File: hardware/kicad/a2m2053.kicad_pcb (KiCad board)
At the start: 2 copper layers, 100 x 110 mm, 46 parts, among them J1 DB-19 female R/A (daisy chain), J2 CN104 mechanism, J3 CN102 host (FROM HOST), J4 Eject button, J5 In-use LED, U1 SN74LVC8T245DWR, U2 SN74LVC8T245DWR, U3 SN74LVC8T245DWR, U4 SN74LVC8T245DWR, U5 SN74LVC8T245DWR

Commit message: fix(pcb): remove two dangling vias left from hand edits
Co-Authored-By: Claude Fable 5.1 <noreply@anthropic.com>
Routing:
- net +12V: track 99.3 -> 102.9 mm
- net /PH0_A: vias 1 -> 0
- net /LED_B: vias 1 -> 0
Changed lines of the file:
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@@
 	)
 	(via
-		(at 139.825 77.6609)
+		(at 139.8 74.2)
 		(size 1)
 		(drill 0.5)
@@
 	)
 	(segment
-		(start 139.825 77.6609)
-		(end 141.2 77.6609)
+		(start 141.2 77.6609)
+		(end 141.2 76.22)
 		(width 1)
 		(layer "B.Cu")
@@
 	)
 	(segment
-		(start 141.2 77.6609)
-		(end 170.5259 77.6609)
+		(start 128.92 74.22)
+		(end 126.38 74.22)
 		(width 1)
 		(layer "B.Cu")
@@
 	)
 	(segment
-		(start 128.92 74.22)
-		(end 126.38 74.22)
+		(start 141.2 76.22)
+		(end 139.2 74.22)
 		(width 1)
 		(layer "B.Cu")
@@
 	(segment
 		(start 131.46 74.22)
-		(end 134.9009 77.6609)
+		(end 139.2 74.22)
 		(width 1)
 		(layer "B.Cu")
@@
 	)
 	(segment
-		(start 180.5766 77.5855)
-		(end 170.6013 77.5855)
+		(start 171.459033 77.5855)
+		(end 169.825 75.951467)
 		(width 1)
 		(layer "B.Cu")
@@
 	)
 	(segment
-		(start 185.9106 72.2515)
-		(end 180.5766 77.5855)
+		(start 139.2 74.22)
+		(end 169.825 74.22)
+		(width 1)
+		(layer "B.Cu")
+		(net "+12V")
+	)
+	(segment
+		(start 169.825 75.951467)
+		(end 169.825 74.22)
 		(width 1)
 		(layer "B.Cu")
@@
 	)
 	(segment
-		(start 170.6013 77.5855)
-		(end 170.6013 75.8387)
+		(start 180.5766 77.5855)
+		(end 171.459033 77.5855)
+		(width 1)
+		(layer "B.Cu")
+		(net "+12V")
+	)
+	(segment
+		(start 185.9106 72.2515)
+		(end 180.5766 77.5855)
 		(width 1)
 		(layer "B.Cu")
@@
 	)
 	(segment
-		(start 170.6013 75.8387)
+		(start 172.22 74.22)
 		(end 175.39 71.05)
 		(width 1)
@@
 	)
 	(segment
-		(start 134.9009 77.6609)
-		(end 139.825 77.6609)
+		(start 169.825 74.22)
+		(end 172.22 74.22)
 		(width 1)
 		(layer "B.Cu")
@@
 	)
 	(segment
-		(start 170.5259 77.6609)
-		(end 170.6013 77.5855)
-		(width 1)
-		(layer "B.Cu")
-		(net "+12V")
-	)
-	(segment
 		(start 129.325 90.35)
 		(end 129.325 75.8598)
@@
 		(net "/PH0_A")
 	)
-	(via
-		(at 131.2678 144.9024)
-		(size 0.6)
-		(drill 0.3)
-		(layers "F.Cu" "B.Cu")
-		(net "/PH0_A")
-	)
 	(segment
 		(start 130.4121 143.47)
@@
 		(net "/LED_B")
 	)
-	(via
-		(at 137.4625 64.7169)
-		(size 0.6)
-		(drill 0.3)
-		(layers "F.Cu" "B.Cu")
-		(net "/LED_B")
-	)

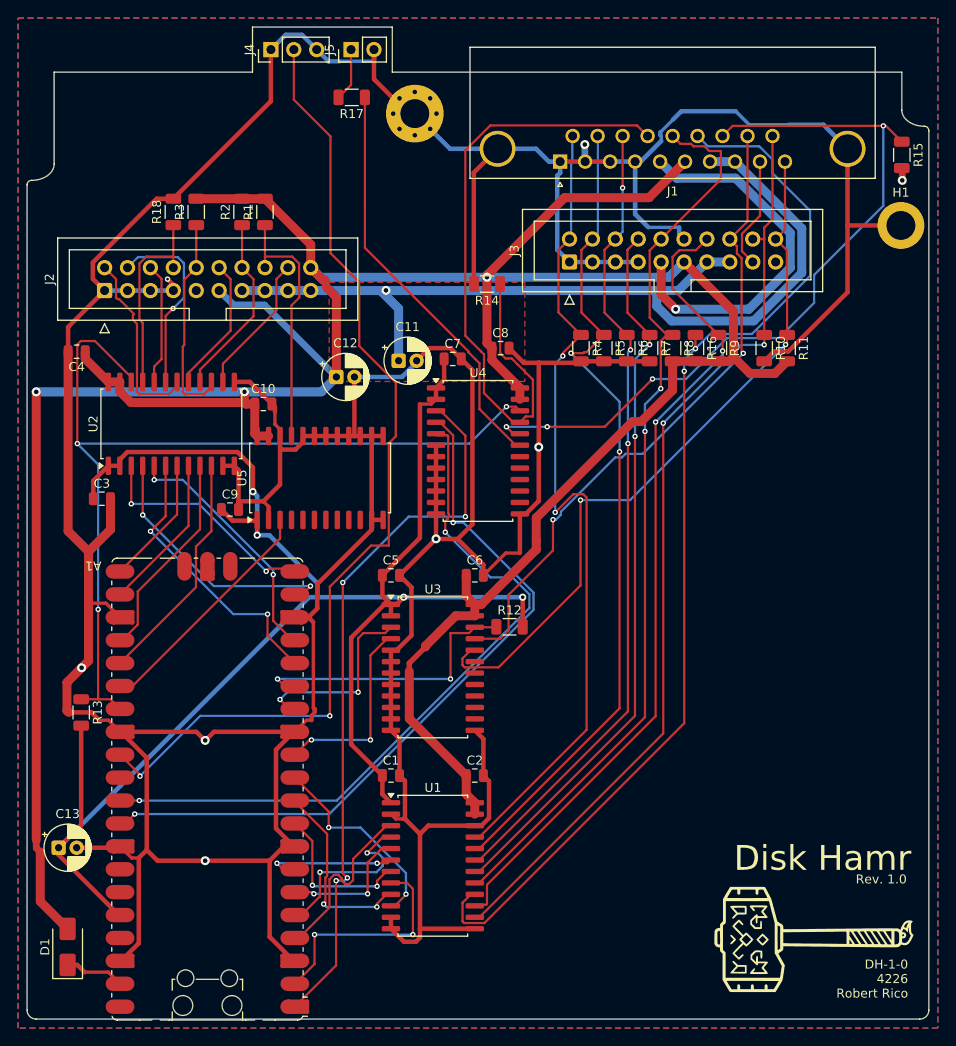
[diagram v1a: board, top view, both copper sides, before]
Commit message: feat(pcb): second layout of Disk Hamr rev 1.0, hand placed, +5V as traces
The 3D print put the mechanism header (J2) 11 mm too far from the
board edge, so the board was placed again by hand and re-routed with
Freerouting, then fixed up by hand.

- Shifters next to the connectors they serve: U2/U5 by J2, U1/U3/U4
  under J1/J3, Pico along the left edge.
- +5V pour on F.Cu removed. +5V is a Power net class now (1 mm
  track, 1 mm via) and is routed as traces; the pour had split into
  eleven islands under the signal traces and Freerouting treats a
  plane as already connected.
- +12V zone moved to B.Cu. GND stays a B.Cu plane; a fenced GND pocket
  under J1 is bridged with a top-side jumper.
- J4 (eject, 3-pin) and J5 (LED, 2-pin) swapped to the IF-83's order,
  shroud open toward the board edge. New TE AMP CT 2.00 mm footprints
  with the vendor STEP models (models are local, see docs/SOURCES.md).
- Logo footprint G1 re-placed from the library with the board-only
  attribute so Update PCB from Schematic leaves it alone.
- DRC with zone refill: 0 errors, 0 unconnected. 768 segments,
  123 vias.
- Top and bottom renders in hardware/kicad/render/.
- .gitignore: vendor 3D models and Freerouting .rules files.

Co-Authored-By: Claude Fable 5.1 <noreply@anthropic.com>
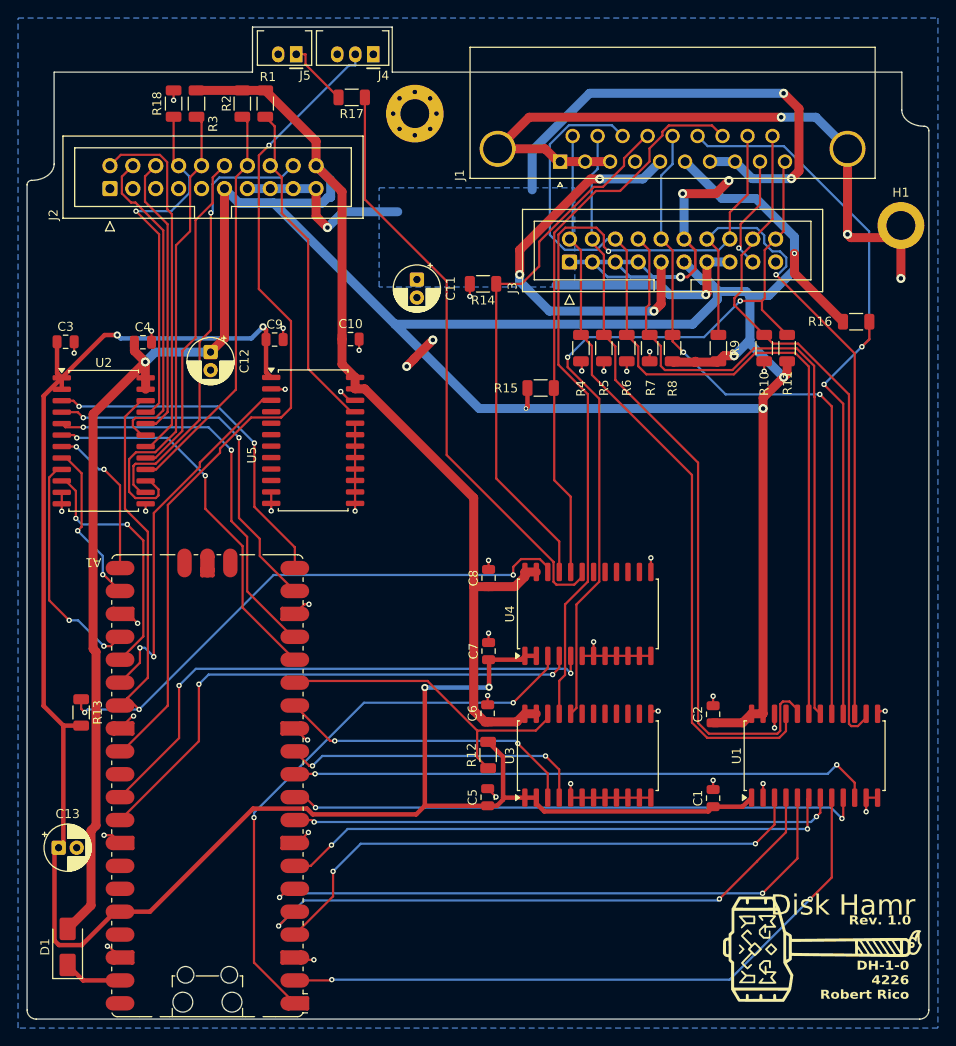
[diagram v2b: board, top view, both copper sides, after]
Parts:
- removed G1: logo_sm, a2m2053:logo_sm
- added G***: LOGO, a2m2053:logo_sm, F.Cu at (188.2, 147.2)
- J4: footprint Connector_PinHeader_2.54mm:PinHeader_1x03_P2.54mm_Vertical -> a2m2053:TE_AMP_CT_1x03_P2.00mm_Vertical
- J5: footprint Connector_PinHeader_2.54mm:PinHeader_1x02_P2.54mm_Vertical -> a2m2053:TE_AMP_CT_1x02_P2.00mm_Vertical
- moved R15 47.7 mm to (156.9, 85.0), turned to 180 degrees
- moved U1 44.1 mm to (187.3, 125.8), turned to 90 degrees
- moved C1 35.8 mm to (176.1, 130.5), turned to 90 degrees
- moved C7 32.6 mm to (151.2, 114.2), turned to 90 degrees
- moved C2 27.3 mm to (176.1, 121.2), turned to 90 degrees
- moved C5 26.8 mm to (151.1, 130.4), turned to 90 degrees
- moved C8 25.5 mm to (151.2, 106.1), turned to 90 degrees
- moved U4 21.8 mm to (162.2, 110.1), turned to 90 degrees
- moved U3 19.8 mm to (162.2, 125.8), turned to 90 degrees
- moved C9 19.5 mm to (127.5, 79.7)
- moved R16 18.1 mm to (191.9, 77.7), turned to 180 degrees
- moved C3 17.9 mm to (104.3, 79.9)
- moved C6 15.4 mm to (151.1, 121.1), turned to 90 degrees
- moved R12 14.4 mm to (151.1, 125.7), turned to 90 degrees
- moved C12 14.2 mm to (120.3, 81.0), turned to -90 degrees
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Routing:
- net GND: track 653.2 -> 212.4 mm, vias 7 -> 47
- net +5V: track 355.7 -> 436.2 mm, vias 4 -> 6
- net /PH2_A: track 14.8 -> 68.0 mm
- net /LASTONE_A: track 25.1 -> 73.1 mm
- net /PH1_A: track 19.8 -> 66.9 mm
- net /PH3_A: track 15.0 -> 62.1 mm
- net /WRREQ_A: track 17.5 -> 60.5 mm
- net /PH0_A: track 20.0 -> 62.9 mm, vias 0 -> 2
- net /WR_A: track 22.3 -> 65.0 mm
- net /HSTEN_A: track 21.5 -> 64.0 mm
- net /LASTONE: track 121.3 -> 83.0 mm
- net /MECH_WRTDATA: track 15.7 -> 49.7 mm, vias 0 -> 1
- net /MECH_WRTGATE: track 23.2 -> 52.5 mm
- net +3V3: track 197.7 -> 225.2 mm
- net /HOST_WR: track 103.3 -> 76.7 mm, vias 2 -> 0
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- added copper zone on B.Cu, net +12V
- removed copper zone on F.Cu, net +12V
- removed copper zone on F.Cu, net +5V

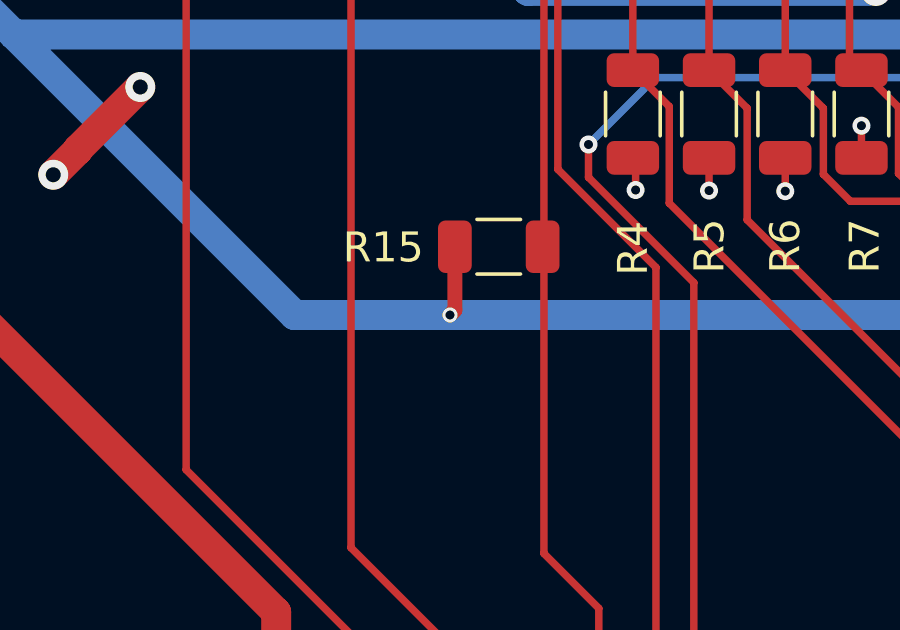
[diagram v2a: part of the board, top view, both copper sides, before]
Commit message: fix(pcb): R17 is 180 ohm, the IF-83's LED anode pull-up
Measured the LED pull-up on the IF-83: 180 ohm to +5V. Our board drives
the LED the same way (U4 output through R17, cathode to GND), so R17
takes the same value for the same brightness. About 17 mA from 5 V,
inside the 8T245's 32 mA output rating.

- Schematic and board: R17 value 330 -> 180. Footprint unchanged, so
  the fabrication outputs are unaffected.
- bom.csv / bom.md: R17 = 180 (Yageo RC1206FR-07180RL, DigiKey
  311-180FRCT-ND); the "keep 220 and 470 on hand" note is gone and the
  open item on the R17 value is closed.
- FABRICATION.md and research_notes.md record the measurement,
  2026-10-25.

Co-Authored-By: Claude Fable 5.1 <noreply@anthropic.com>
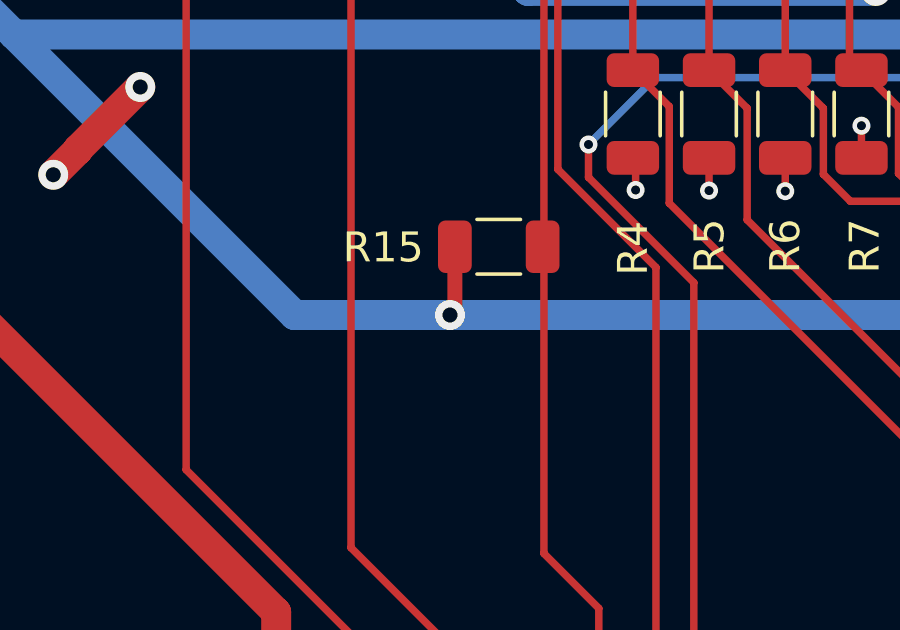
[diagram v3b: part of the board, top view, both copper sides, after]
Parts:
- R17: value 330 -> 180
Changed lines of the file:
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@@
 			(outputformat 1)
 			(mirror no)
-			(drillshape 1)
+			(drillshape 0)
 			(scaleselection 1)
-			(outputdirectory "")
+			(outputdirectory "fabrication/")
 		)
 	)
@@
 			)
 		)
-		(property "Value" "330"
+		(property "Value" "180"
 			(at 0 1.83 180)
 			(layer "F.Fab")
@@
 	(via
 		(at 155.325 87.3)
-		(size 0.5)
-		(drill 0.3)
+		(size 1)
+		(drill 0.5)
 		(layers "F.Cu" "B.Cu")
 		(net "+5V")

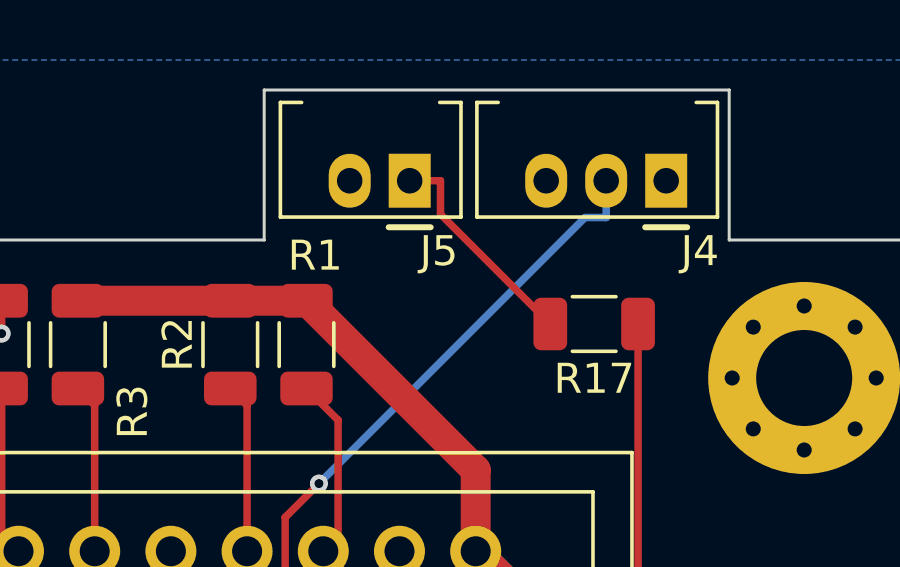
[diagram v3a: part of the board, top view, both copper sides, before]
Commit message: fix(pcb): swap J5 pins to match the IF-83 LED header, re-plot Gerbers
Measured on the IF-83 (2026-10-25): the CN107 pin nearer the 3-pin eject
header goes to the Q101 sink (cathode side); the far pin carries the
180 ohm pull-up to +5V (anode side). Our J5 had /LED on the near pin and
GND on the far pin, so the drive's own LED lead would have sat
reverse-biased.

- Schematic and board: J5 pin 1 (nearer J4) is GND, pin 2 (toward the
  board edge) is /LED through R17. Two stubs re-routed. DRC: 0 errors,
  0 unconnected.
- Gerbers and drills re-plotted with kicad-cli, same layer set and
  formats as the 08:38 plot. Zip disk_hamr_2026_10_25b.zip replaces the
  earlier upload; the first zip has J5 mirrored.
- FABRICATION, HANDOFF, bom.md and research_notes record the measurement
  and the fix.

Co-Authored-By: Claude Fable 5.1 <noreply@anthropic.com>
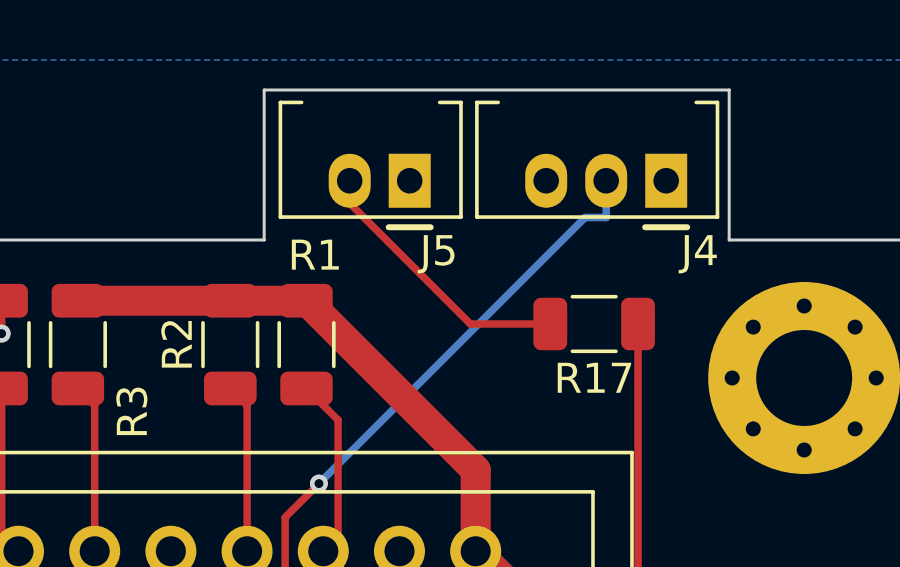
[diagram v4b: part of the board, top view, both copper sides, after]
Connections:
- J5 pad 1: /LED -> GND
- J5 pad 2: GND -> /LED
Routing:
- net /LED: track 7.32 -> 9.10 mm
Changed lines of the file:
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@@
 			(layers "*.Cu" "*.Mask")
 			(remove_unused_layers no)
-			(net "/LED")
+			(net "GND")
 			(pinfunction "Pin_1_1")
 			(pintype "passive")
@@
 			(layers "*.Cu" "*.Mask")
 			(remove_unused_layers no)
-			(net "GND")
+			(net "/LED")
 			(pinfunction "Pin_2_2")
 			(pintype "passive")
@@
 	)
 	(segment
-		(start 129.85 48.025)
-		(end 130.8767 48.025)
+		(start 131.875 52.8)
+		(end 134.5375 52.8)
 		(width 0.25)
 		(layer "F.Cu")
@@
 	)
 	(segment
-		(start 130.8767 48.025)
-		(end 130.8767 49.1392)
+		(start 127.85 48.025)
+		(end 127.85 48.775)
 		(width 0.25)
 		(layer "F.Cu")
@@
 	)
 	(segment
-		(start 130.8767 49.1392)
-		(end 134.5375 52.8)
+		(start 127.85 48.775)
+		(end 131.875 52.8)
 		(width 0.25)
 		(layer "F.Cu")
